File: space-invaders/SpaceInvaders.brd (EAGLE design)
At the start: 92.7 x 81.3 mm, 26 parts

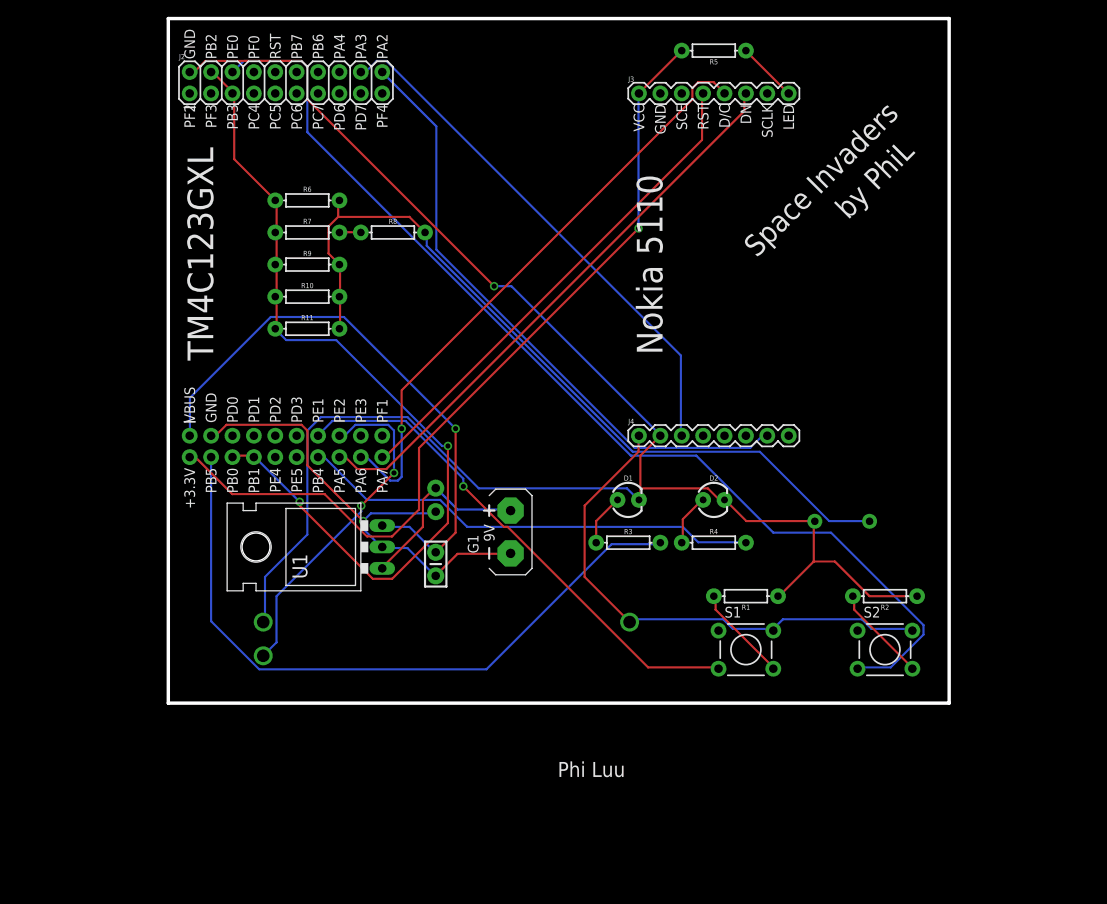
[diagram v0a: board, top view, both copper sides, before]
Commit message: Complete board - SpaceInvaders 2.0
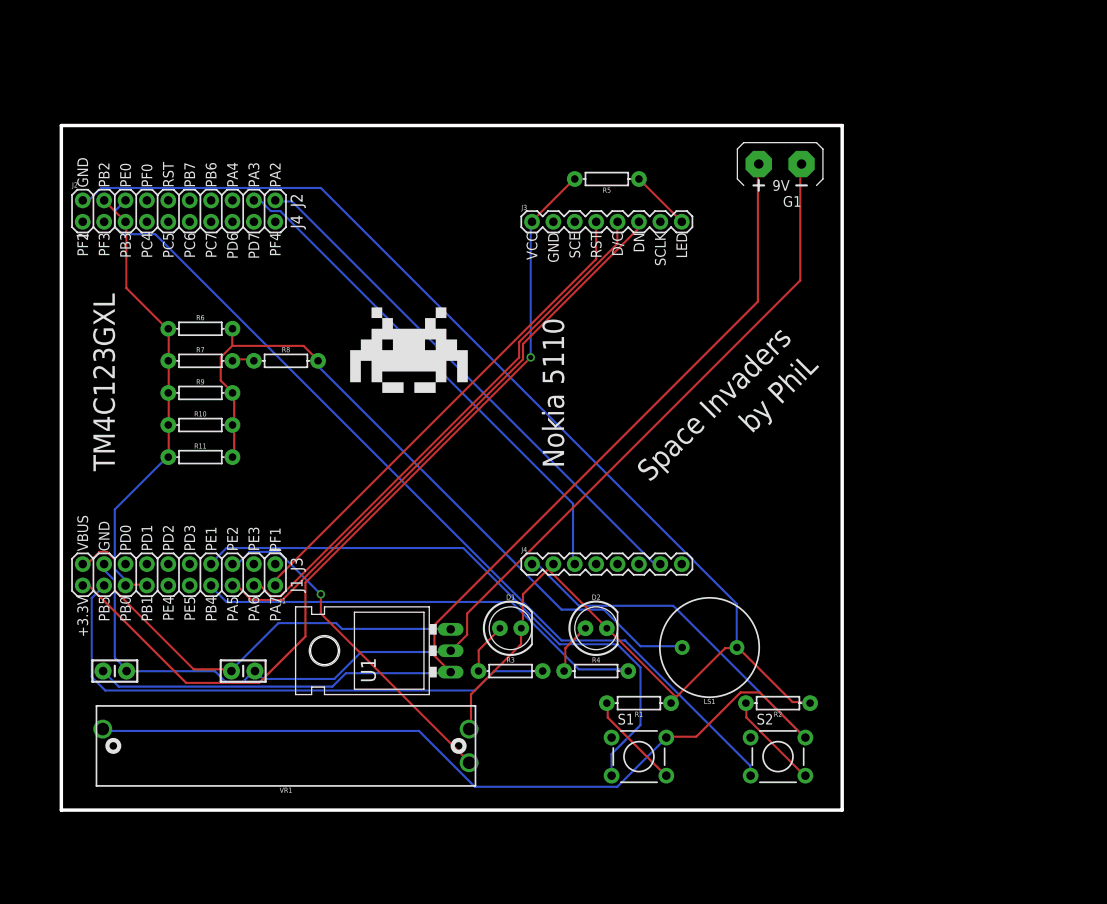
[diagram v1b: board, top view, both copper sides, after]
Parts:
- D1: value (none) -> YELLOW; device SparkFun-LED:LED_3MM -> SparkFun-LED:LED_5MM
- D2: value (none) -> RED; device SparkFun-LED:LED_3MM -> SparkFun-LED:LED_5MM
- J1: value (none) -> TM4C123GXL - J3 & J1
- J2: value (none) -> TM4C123GXL - J2 & J4
- J3, J4: value (none) -> Nokia 5110
- S1: value (none) -> Left Switch
- S2: value (none) -> Right Switch
- U1: value (none) -> 5V Voltage Regulator
- moved G1 54.2 mm to (90.4, 85.6), turned to 90 degrees
- moved C2 43.2 mm to (11.4, 25.4), flipped to the top, turned to 0 degrees
- moved C1 26.2 mm to (26.7, 25.4), turned to 180 degrees
- moved VR1 22.9 mm to (31.8, 16.5), flipped to the top
- moved LS1 21.7 mm to (82.0, 28.2), flipped to the top
- moved R3 20.7 mm to (58.4, 25.4)
- moved R4 20.7 mm to (68.6, 25.4)
- moved D1 20.7 mm to (58.4, 30.5)
- moved D2 20.7 mm to (68.6, 30.5)
- moved R5 19.8 mm to (69.8, 83.8)
- moved J2 19.8 mm to (7.62, 78.7)
- moved R11 19.8 mm to (21.6, 50.8)
- moved J3 19.8 mm to (61.0, 78.7)
- moved R8 19.8 mm to (31.8, 62.2)
- moved R7 19.8 mm to (21.6, 62.2)
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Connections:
- net N$12: now also J1.2; no longer J1.20
- net N$13: now also J1.4; no longer J1.18
- net N$15: now also J1.6; no longer J1.16
- net N$17: now also J1.5; no longer J1.15
- net N$19: now also J1.7; no longer J1.13
- net N$21: now also J1.18; no longer J1.4
- net N$22: now also J1.8; no longer J1.14
- net N$24: now also J1.19; no longer J1.1
- net N$25: now also J1.17; no longer J1.3
- net N$5: now also J1.14, J1.16; no longer J1.6, J1.8
- net N$9: now also J1.20; no longer J1.2
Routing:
- net N$23: track 22.2 -> 119.8 mm
- net N$25: track 56.8 -> 130.3 mm, vias 1 -> 0
- net N$10: track 62.5 -> 134.2 mm
- net N$5: track 105.0 -> 54.9 mm, vias 2 -> 0
- net N$11: track 202.1 -> 172.3 mm, vias 1 -> 0
- net N$20: track 125.6 -> 106.8 mm
- net N$21: track 81.5 -> 66.6 mm
- net N$24: track 68.9 -> 55.0 mm, vias 1 -> 0
- net N$19: track 61.0 -> 72.0 mm, vias 1 -> 0
- net N$4: track 95.3 -> 85.5 mm
- net N$16: track 73.4 -> 63.6 mm
- net N$13: track 71.3 -> 64.7 mm, vias 1 -> 0
- net N$14: track 62.6 -> 60.1 mm
- net N$9: track 99.9 -> 101.1 mm
- net N$22: track 55.0 -> 53.8 mm
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- added copper zone on layer 1, net N$18
- removed copper zone on layer 1, net GND
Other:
- board text added: "J1"
- board text added: "J2"
- board text added: "J3"
- board text added: "J4"

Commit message: Add silkscreen & Finish SpaceInvaders
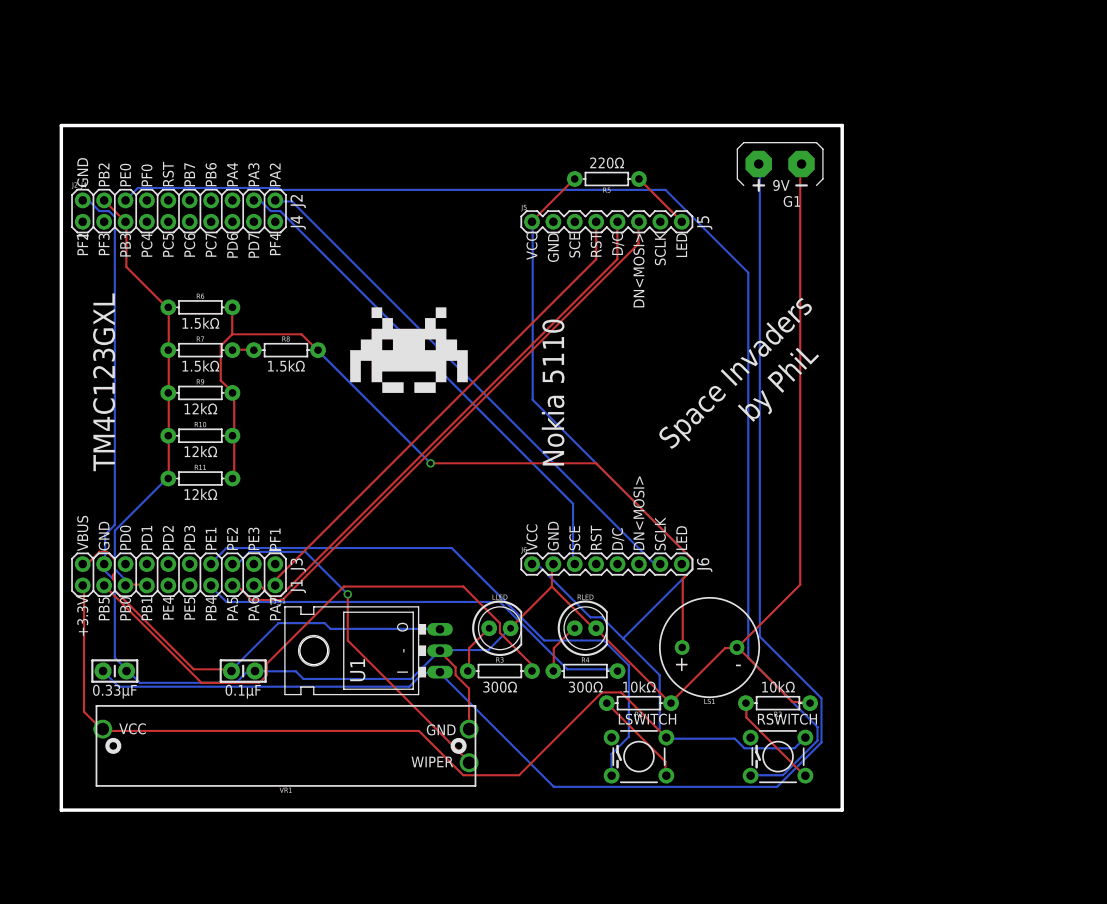
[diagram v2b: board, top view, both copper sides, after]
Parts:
- removed D1: YELLOW, SparkFun-LED:LED_5MM
- removed D2: RED, SparkFun-LED:LED_5MM
- added LLED: YELLOW, SparkFun-LED:LED_5MM
- added RLED: RED, SparkFun-LED:LED_5MM
- C1: value 0.1uF -> 0.1μF
- C2: value 0.33uF -> 0.33μF
- J2_J4: value TM4C123GXL - J2 & J4 -> TM4C123GXL
- J3_J1: value TM4C123GXL - J3 & J1 -> TM4C123GXL
- LSWITCH: value Left Switch -> TACTILE
- R1, R2, VR1: value 10k -> 10kΩ
- R10, R11, R9: value 12k -> 12kΩ
- R3, R4: value 300 -> 300Ω
- R5: value 220 -> 220Ω
- R6, R7, R8: value 1.5k -> 1.5kΩ
- RSWITCH: value Right Switch -> TACTILE
- moved R11 2.54 mm to (21.6, 48.3)
- moved R6 2.54 mm to (21.6, 68.6)
- moved R3 1.27 mm to (57.1, 25.4)
- moved R7 1.27 mm to (21.6, 63.5)
- moved R8 1.27 mm to (31.8, 63.5)
- moved R10 1.27 mm to (21.6, 53.3)
- moved R4 1.27 mm to (67.3, 25.4)
- moved U1 1.27 mm to (46.2, 27.8)
- renumbered J1 to J3_J1, J2 to J2_J4, J3 to J5, J4 to J6, S1 to LSWITCH, S2 to RSWITCH
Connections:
- net N$12 renamed PA7
- net N$13 renamed PA6
- net N$14 renamed PA3
- net N$15 renamed PA5
- net N$16 renamed PA2
- net N$17 renamed PE2
- net N$19 renamed PE1
- net N$20 renamed PE0
- net N$21 renamed PB5
- net N$22 renamed PB4
- net N$24 renamed VBUS
- net N$3 renamed LED
- net N$5 renamed PB2
- removed net N$10: J6.1, LSWITCH.2, RSWITCH.2, VR1.BOTTOM
- removed net N$11: D1.K, D2.K, J2_J4.2, J6.2, LS1.-, R1.P$1, R2.P$1, VR1.TOP
- removed net N$25: C1.1, C2.2, G1.-, J3_J1.17, U1.GND
- removed net N$7: D1.A, R3.P$1
- removed net N$8: D2.A, R4.P$1
- removed net N$9: J3_J1.20, J5.1, R5.P$2
- new net +3.3V: J3_J1.20, J5.1, J6.1, LSWITCH.2, R5.P$2, RSWITCH.2, VR1.BOTTOM
- new net GND: C1.1, C2.2, G1.-, J2_J4.2, J3_J1.17, J6.2, LLED.K, LS1.-, R1.P$1, R2.P$1, RLED.K, U1.GND, VR1.TOP
- new net N$17: R4.P$1, RLED.A
- new net N$19: LLED.A, R3.P$1
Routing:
- net GND: track 0.00 -> 232.9 mm
- net +3.3V: track 0.00 -> 207.6 mm
- net N$11: track 172.3 -> 0.00 mm
- net N$10: track 134.2 -> 0.00 mm
- net N$25: track 130.3 -> 0.00 mm
- net N$9: track 101.1 -> 0.00 mm, vias 1 -> 0
- net N$24: track 119.8 -> 166.4 mm
- net PE0: track 106.8 -> 147.3 mm
- net N$23: track 85.5 -> 98.6 mm, vias 0 -> 1
- net N$17: track 0.00 -> 6.17 mm
- net N$8: track 6.13 -> 0.00 mm
- net N$19: track 0.00 -> 6.13 mm
- net N$7: track 6.12 -> 0.00 mm
- net PE2: track 40.5 -> 42.3 mm
- net PE1: track 72.0 -> 70.1 mm
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- added copper zone on layer 1, net GND
- removed copper zone on layer 1, net N$18
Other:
- board text added: "+"
- board text added: "-"
- board text added: "0.1μF"
- board text added: "0.33μF"
- board text added: "1.5kΩ"
- board text added: "10kΩ"
- board text added: "12kΩ"
- board text added: "220Ω"
- board text added: "300Ω"
- board text added: "DN<MOSI>"
- board text added: "I"
- board text added: "J5"
- board text added: "J6"
- board text added: "O"
- board text added: "WIPER"
- board text removed: "DN"

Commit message: Setup SpaceInvaders regular manufacturing
Default EAGLE Design Rule Check (DRC). Double sided.
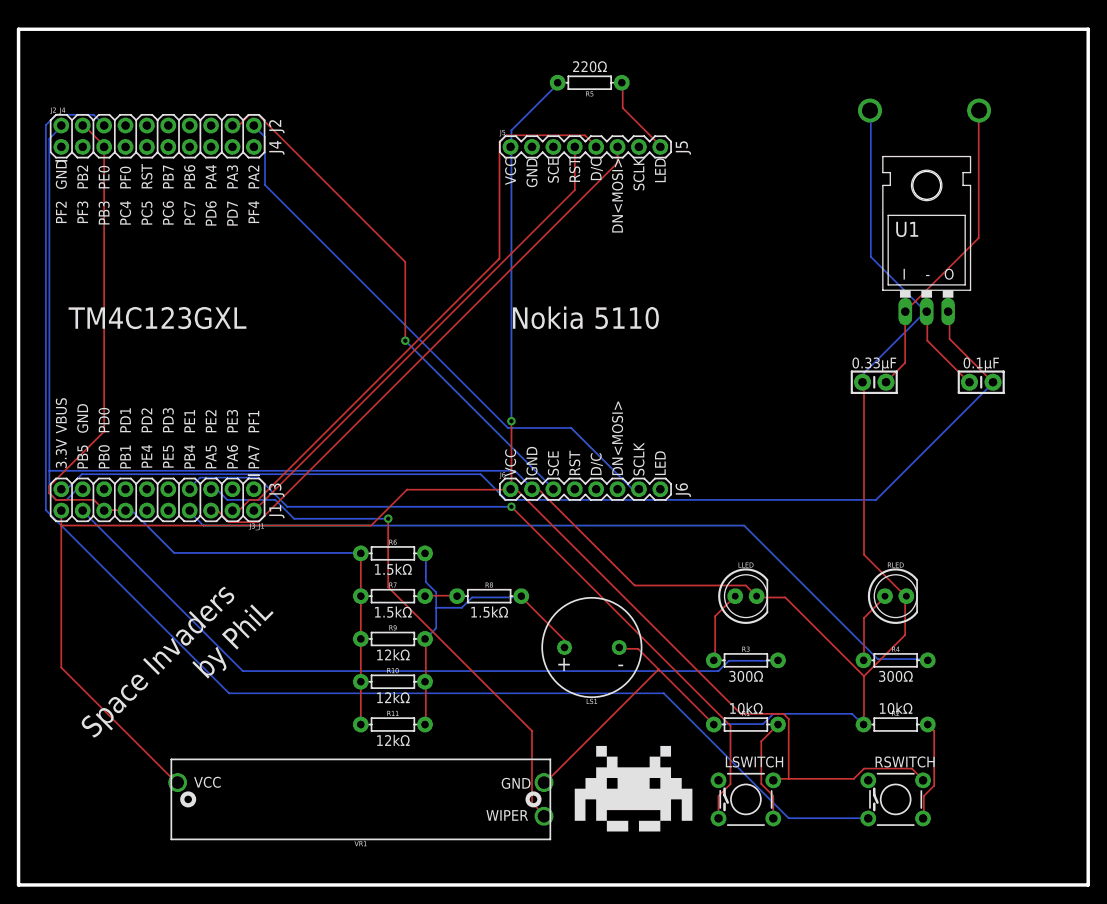
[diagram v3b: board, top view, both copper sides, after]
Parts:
- G1: value AB9V -> 9V; device battery:AB9V -> SparkFun-Batteries:BATTCON_9V
- moved C2 96.5 mm to (101.6, 59.7), turned to 180 degrees
- moved C1 94.1 mm to (114.3, 59.7), turned to 0 degrees
- moved U1 75.7 mm to (107.8, 71.9), turned to 0 degrees
- moved R8 37.9 mm to (55.9, 34.3)
- moved R10 37.1 mm to (44.5, 24.1)
- moved R6 37.1 mm to (44.5, 39.4)
- moved R7 37.1 mm to (44.5, 34.3)
- moved R9 37.1 mm to (44.5, 29.2)
- moved R11 37.1 mm to (44.5, 19.1)
- moved RLED 37.0 mm to (104.1, 34.3)
- moved R4 36.9 mm to (104.1, 26.7)
- moved LLED 29.5 mm to (86.4, 34.3)
- moved R3 29.2 mm to (86.4, 26.7)
- moved G1 24.5 mm to (114.0, 91.9), flipped to the bottom
- moved RSWITCH 14.9 mm to (104.1, 10.2)
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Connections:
- net +3.3V renamed 3.3V
- net N$12 renamed LSWITCH_GND
- net N$14 renamed RSWITCH_GND
- net N$17 renamed RLED
- net N$19 renamed LLED
- net N$23 renamed DAC_OUT
- net N$24 renamed 9V
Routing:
- net 9V: track 166.4 -> 36.8 mm
- net VBUS: track 53.9 -> 129.2 mm
- net GND: track 232.9 -> 302.9 mm
- net DAC_OUT: track 98.6 -> 40.5 mm, vias 1 -> 0
- net PB2: track 55.0 -> 107.9 mm
- net PB4: track 52.6 -> 95.1 mm
- net PB5: track 66.4 -> 91.0 mm
- net PE2: track 42.3 -> 65.5 mm
- net PE0: track 147.3 -> 166.5 mm
- net PE1: track 70.1 -> 88.7 mm, vias 0 -> 1
- net 3.3V: track 207.6 -> 214.4 mm, vias 0 -> 1
- net PA6: track 64.7 -> 70.3 mm
- net PA2: track 63.6 -> 67.0 mm
- net LLED: track 6.13 -> 8.67 mm
- net RLED: track 6.17 -> 8.65 mm
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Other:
- board size 92.7 x 81.3 mm -> 127 x 101.6 mm
- board text added: "3.3V"
- board text removed: "+3.3V"

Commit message: Update board SpaceInvaders
Add names to empty pins
Naming convention
Change switch package
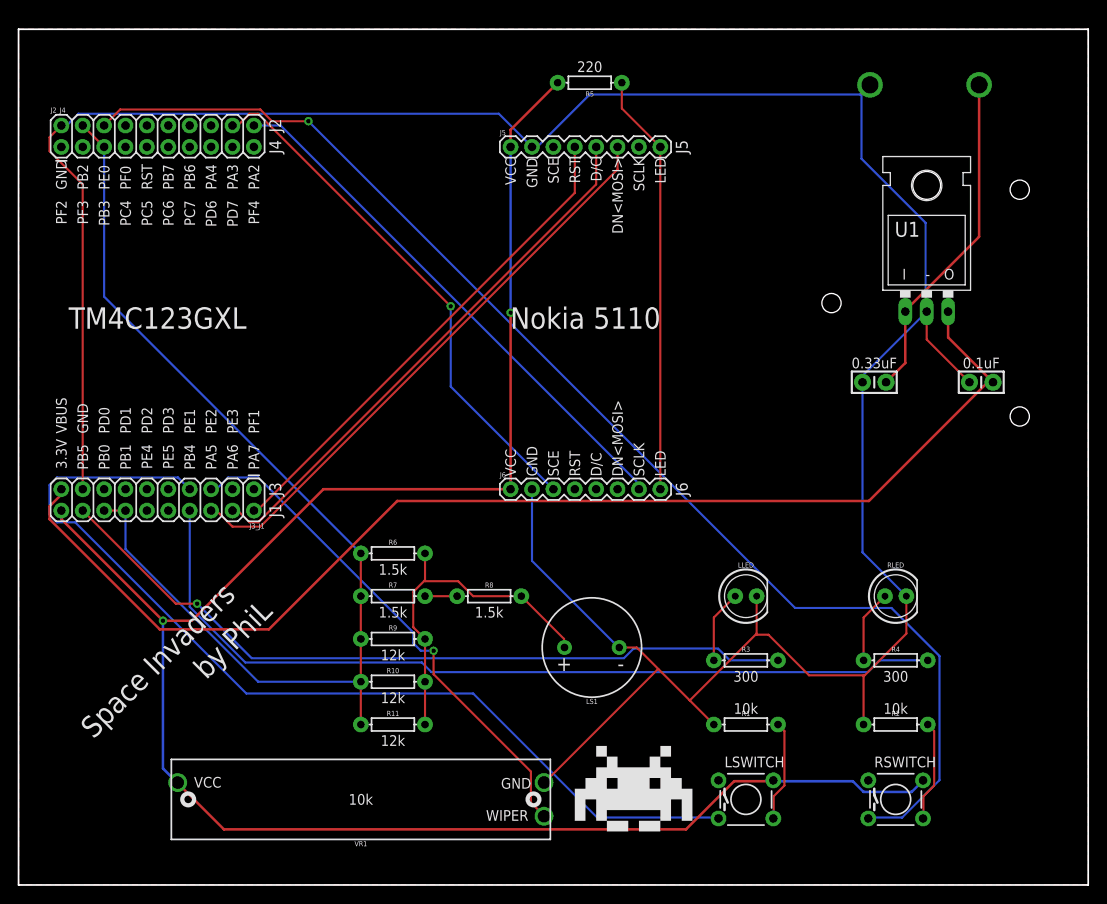
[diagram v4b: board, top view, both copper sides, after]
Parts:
- removed G1: 9V, SparkFun-Batteries:BATTCON_9V
- added J1: 9V, SparkFun-Connectors:BC9VPC
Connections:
- new net D/C: J6.5
- new net DN<MOSI>: J6.6
- new net PA4: J2_J4.16
- new net PB6: J2_J4.14
- new net PB7: J2_J4.12
- new net PC4: J2_J4.7
- new net PC5: J2_J4.9
- new net PC6: J2_J4.11
- new net PC7: J2_J4.13
- new net PD0: J3_J1.15
- new net PD1: J3_J1.13
- new net PD2: J3_J1.11
- new net PD3: J3_J1.9
- new net PD6: J2_J4.15
- new net PD7: J2_J4.17
- new net PE3: J3_J1.3
- new net PE4: J3_J1.12
- new net PE5: J3_J1.10
- new net PF0: J2_J4.8
- new net PF1: J3_J1.1
- new net PF2: J2_J4.1
- new net PF3: J2_J4.3
- new net PF4: J2_J4.19
- new net RESET: J2_J4.10
- new net RST: J6.4
- new net SCE: J5.3
- new net SCLK: J5.7
- net 9V: now also J1.V+; no longer G1.+
- net GND: now also J1.V-, J5.2; no longer G1.-
- net LED: now also J6.8
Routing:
- net LED: track 9.50 -> 50.2 mm
- net GND: track 302.9 -> 330.6 mm
- net PE1: track 88.7 -> 115.5 mm, vias 1 -> 0
- net PB2: track 107.9 -> 126.4 mm
- net 3.3V: track 214.4 -> 230.8 mm, vias 1 -> 2
- net VBUS: track 129.2 -> 144.5 mm
- net PE0: track 166.5 -> 151.9 mm, vias 0 -> 1
- net PB4: track 95.1 -> 102.8 mm
- net PA6: track 70.3 -> 64.8 mm
- net PE2: track 65.5 -> 61.3 mm
- net 9V: track 36.8 -> 39.9 mm
- net PA2: track 67.0 -> 64.0 mm
- net DAC_OUT: track 40.5 -> 42.0 mm
- net PA5: track 68.4 -> 69.3 mm
- net LSWITCH_GND: track 12.6 -> 12.0 mm
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- added copper zone on layer 1, net N$2
- removed copper zone on layer 1, net GND
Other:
- board text added: "0.1uF"
- board text added: "0.33uF"
- board text added: "1.5k"
- board text added: "10k"
- board text added: "12k"
- board text added: "220"
- board text added: "300"
- board text removed: "0.1μF"
- board text removed: "0.33μF"
- board text removed: "1.5kΩ"
- board text removed: "10kΩ"
- board text removed: "12kΩ"
- board text removed: "220Ω"
- board text removed: "300Ω"
